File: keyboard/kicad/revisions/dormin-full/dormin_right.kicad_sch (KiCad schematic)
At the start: 104 parts, among them J6_R1 Conn_01x04, Q3_R1 AO3407A, Q4_R1 AO3400A, SW21 SW_Push, SW22 SW_Push, SW23 SW_Push, SW24 SW_Push, SW25 SW_Push, SW26 SW_Push, SW27 SW_Push, SW28 SW_Push, SW29 SW_Push, SW30 SW_Push, SW31 SW_Push, SW32 SW_Push, SW33 SW_Push, SW34 SW_Push, SW35 SW_Push, SW36 SW_Push, SW37 SW_Push, SW38 SW_Push, SW39 SW_Push, SW40 SW_Push, U2 Seeeduino Xiao nRF52840

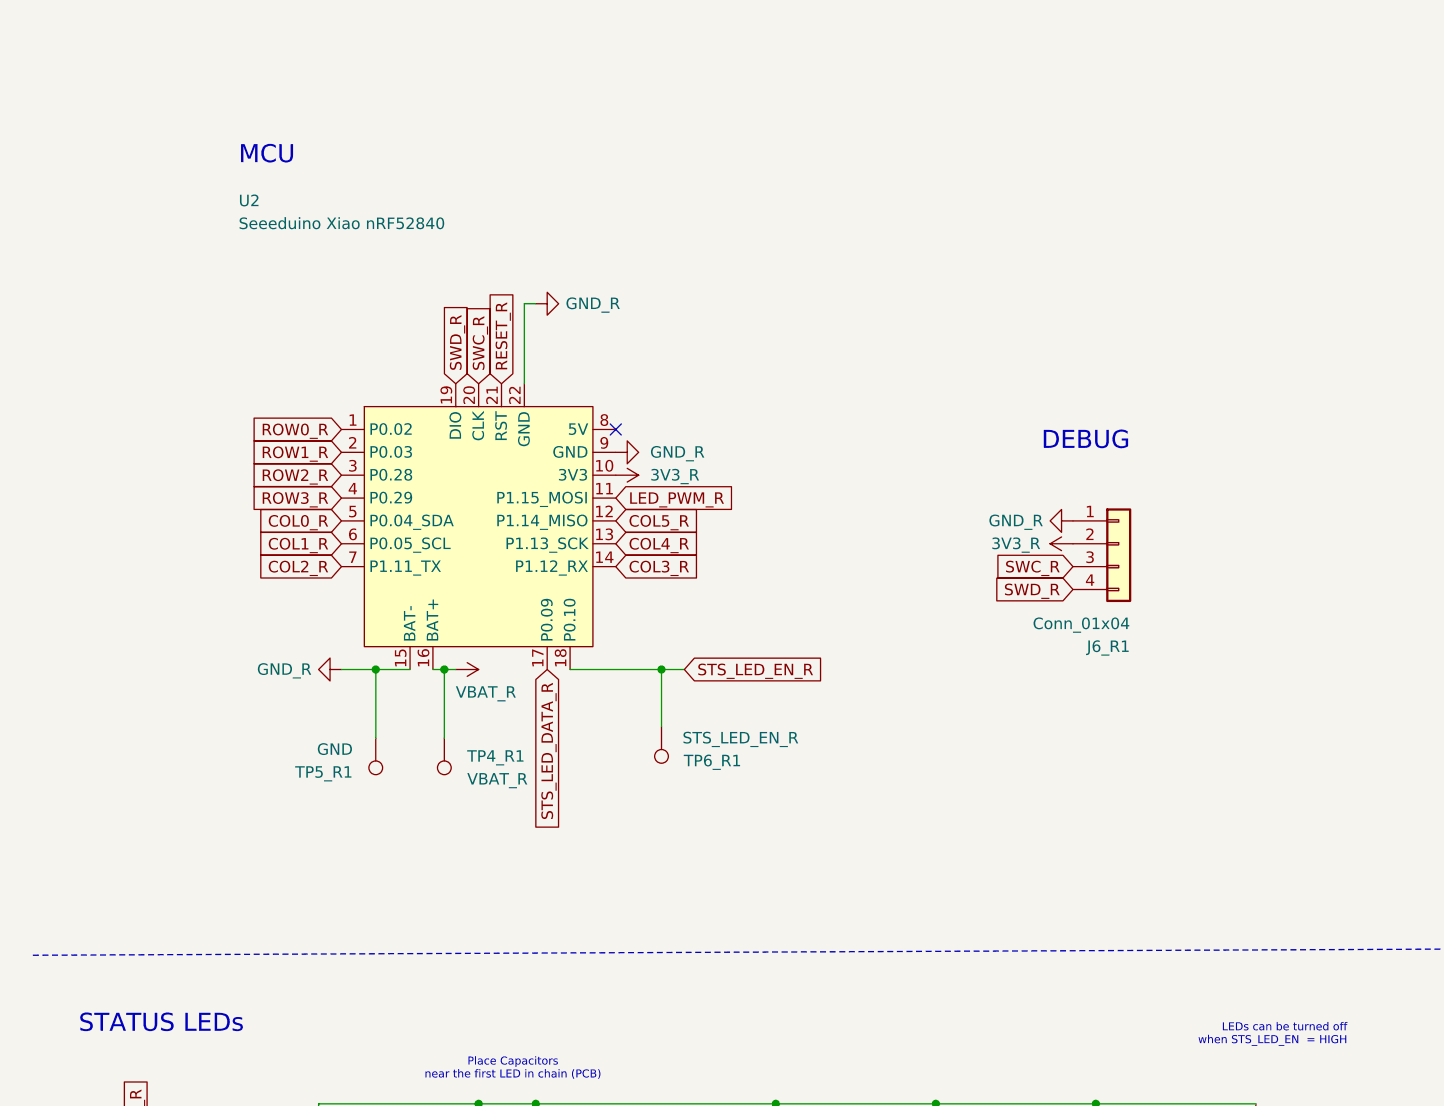
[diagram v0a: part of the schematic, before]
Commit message: feat: remove unused components for v1
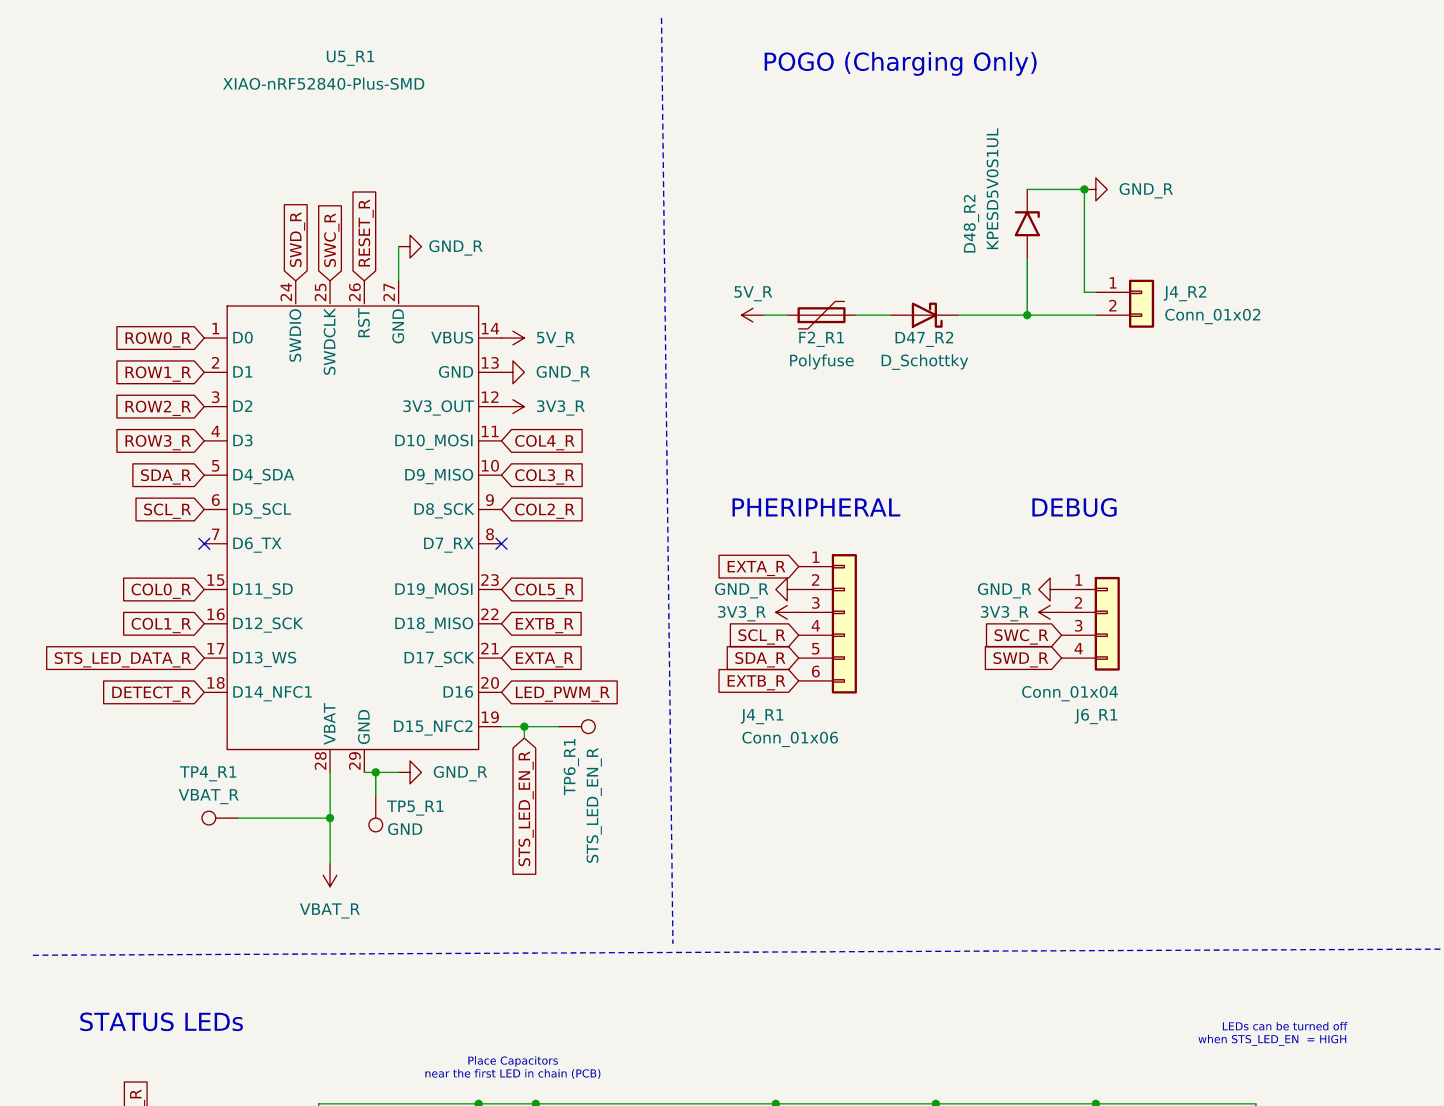
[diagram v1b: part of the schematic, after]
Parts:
- removed U2: Seeeduino Xiao nRF52840, Seeed_Studio_XIAO_Series:XIAO-nRF52840-SMD, symbol PCM_marbastlib-promicroish:Seeeduino_Xiao_nRF52840
- added D47_R2: D_Schottky, Diode_SMD:D_SOD-523, symbol Device:D_Schottky
- added D48_R2: KPESD5V0S1UL, Diode_SMD:D_SOD-882, symbol Diode:SMF5V0A
- added F2_R1: Polyfuse, Fuse:Fuse_1206_3216Metric, symbol Device:Polyfuse
- added J4_R1: Conn_01x06, willkeebs_misc:SMD_Conn_1x06_P2.54mm_Vertical, symbol Connector_Generic:Conn_01x06
- added J4_R2: Conn_01x02, willkeebs_components:Pogo1x2-Right-Angle, symbol Connector_Generic:Conn_01x02
- added U5_R1: XIAO-nRF52840-Plus-SMD, Seeed_Studio_XIAO_Series:XIAO-nRF52840-Plus-SMD, symbol Seeed_Studio_XIAO_Series:XIAO-nRF52840_Plus_SMD
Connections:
- net 3V3_R: now also J4_R1.3 (Pin_3), U5_R1.12 (3V3_OUT)
- net COL0_R: now also U5_R1.15 (D11_SD)
- net COL1_R: now also U5_R1.16 (D12_SCK)
- net COL2_R: now also U5_R1.9 (D8_SCK)
- net COL3_R: now also U5_R1.10 (D9_MISO)
- net COL4_R: now also U5_R1.11 (D10_MOSI)
- net COL5_R: now also U5_R1.23 (D19_MOSI)
- net GND_R: now also D48_R2.1 (A1), J4_R1.2 (Pin_2), J4_R2.1 (Pin_1), U5_R1.13 (GND), U5_R1.27 (GND), U5_R1.29 (GND)
- net LED_PWM_R: now also U5_R1.20 (D16)
- net RESET_R: now also U5_R1.26 (RST)
- net ROW0_R: now also U5_R1.1 (D0)
- net ROW1_R: now also U5_R1.2 (D1)
- net ROW2_R: now also U5_R1.3 (D2)
- net ROW3_R: now also U5_R1.4 (D3)
- net STS_LED_DATA_R: now also U5_R1.17 (D13_WS)
- net STS_LED_EN_R: now also U5_R1.19 (D15_NFC2)
- net SWC_R: now also U5_R1.25 (SWDCLK)
- net SWD_R: now also U5_R1.24 (SWDIO)
- net VBAT_R: now also U5_R1.28 (VBAT)
- new net: D47_R2.1 (K), D48_R2.2 (A2), J4_R2.2 (Pin_2)
- new net: D47_R2.2 (A), F2_R1.2
- new net 5V_R: F2_R1.1, U5_R1.14 (VBUS)
- new net DETECT_R: U5_R1.18 (D14_NFC1)
- new net EXTA_R: J4_R1.1 (Pin_1), U5_R1.21 (D17_SCK)
- new net EXTB_R: J4_R1.6 (Pin_6), U5_R1.22 (D18_MISO)
- new net SCL_R: J4_R1.4 (Pin_4), U5_R1.6 (D5_SCL)
- new net SDA_R: J4_R1.5 (Pin_5), U5_R1.5 (D4_SDA)
- no-connect marks 3 -> 4
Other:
- note added: "PHERIPHERAL"
- note added: "POGO (Charging Only)"
- note removed: "MCU"
- moved on the sheet: J6_R1
